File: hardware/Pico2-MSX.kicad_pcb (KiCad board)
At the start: 4 copper layers, 82.9 x 64.6 mm, 63 parts, among them J1 DEBUG, J2 USB_C, SW1 BOOT, U1 MCP4922-ESL, U2 TXB0108PW, U3 W25Q128JVS, U4 W25Q128JVS, U6 RP2350_80QFN, U7 MC74LCX32DTR2G, U8 AMS1117-3.3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

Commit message: Improving the 1v1 circuit
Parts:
- C16, C17: footprint Capacitor_SMD:C_0603_1608Metric -> Additional:C_0603_1608Metric_small
- L1: footprint Inductor_SMD:L_1008_2520Metric -> Additional:L_pol_2016
- moved L1 0.86 mm to (160.1, 80.7)
- moved C17 0.72 mm to (160.1, 82.8)
- moved D3 0.27 mm to (193.5, 87.8)
- moved TP3 0.14 mm to (159.1, 85.2)
- moved C16 0.13 mm to (160.1, 84.5)
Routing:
- net +3V3: track 255.8 -> 258.9 mm
- net +1V1: track 38.1 -> 36.9 mm
- net /VREG_LX: track 5.93 -> 5.18 mm
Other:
- outline, holes or cut-outs redrawn

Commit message: Some optimizations
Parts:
- added kibuzzard-671CD351: G***, kibuzzard-671CD351, F.Cu at (122.1, 81.5)
- added kibuzzard-671CD378: G***, kibuzzard-671CD378, F.Cu at (122.1, 92.6)
- added kibuzzard-671CD39D: G***, kibuzzard-671CD39D, B.Cu at (159.1, 87.6)
- added kibuzzard-671CD496: G***, kibuzzard-671CD496, B.Cu at (125.7, 71.7)
- moved C19 0.20 mm to (163.5, 87.3)
- moved C20 0.20 mm to (163.5, 90.5)
- moved C21 0.20 mm to (163.5, 91.3)
- moved C22 0.20 mm to (163.5, 94.8)
- moved C5 0.20 mm to (150.7, 88.7)
- moved C6 0.20 mm to (150.7, 90.7)
- moved C7 0.20 mm to (150.7, 92.7)
- moved C10 0.20 mm to (154.5, 97.3)
- moved C11 0.20 mm to (154.9, 84.5)
- moved C12 0.20 mm to (156.5, 97.3)
- moved C13 0.20 mm to (157.7, 84.5)
- moved C14 0.20 mm to (157.8, 97.3)
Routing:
- net +3V3: track 258.9 -> 257.1 mm
- net +1V1: track 36.9 -> 36.3 mm

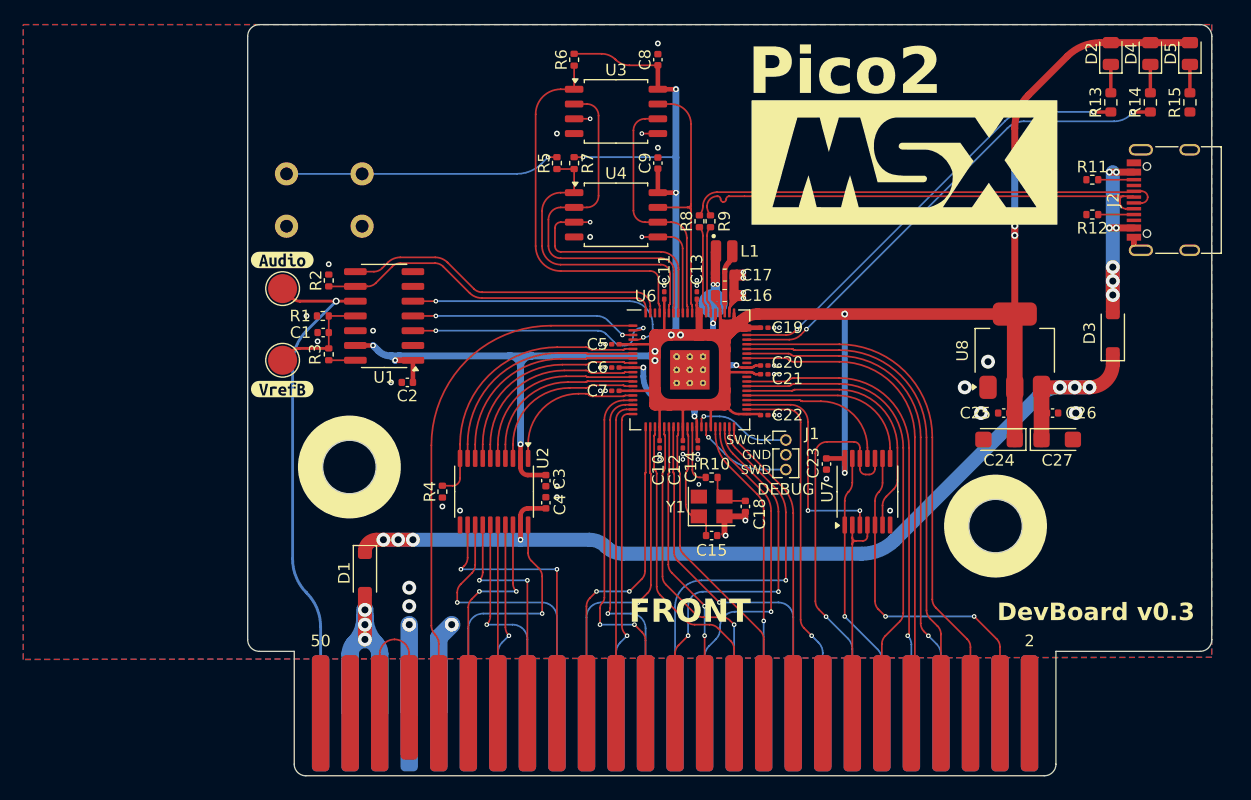
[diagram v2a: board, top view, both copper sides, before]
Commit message: Delete via for flash memory
And other small modifications (reference at JLCPCB)
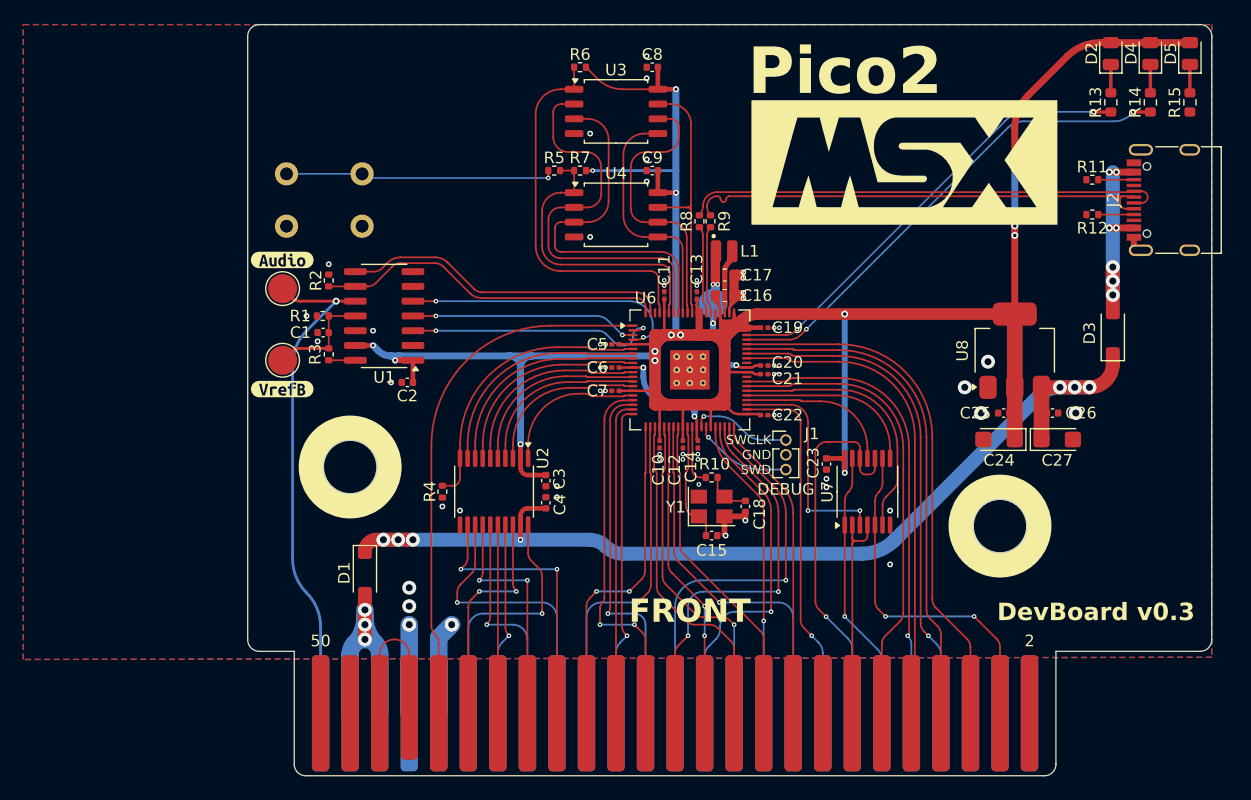
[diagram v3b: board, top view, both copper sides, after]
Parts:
- moved R6 0.82 mm to (147.7, 64.9), turned to 180 degrees
- moved R7 0.82 mm to (147.7, 73.8), turned to 180 degrees
- moved C8 0.80 mm to (153.9, 64.9), turned to 180 degrees
- moved C9 0.80 mm to (153.9, 73.8), turned to 180 degrees
- moved R5 0.68 mm to (145.5, 73.8), turned to 180 degrees
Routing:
- net /QSPI_SD1: track 32.7 -> 35.6 mm
- net /QSPI_SCLK: track 21.8 -> 24.7 mm
- net /QSPI_SD0: track 19.8 -> 21.3 mm, vias 2 -> 0
- net /QSPI_SD2: track 30.5 -> 32.0 mm, vias 2 -> 0
- net +3V3: track 257.1 -> 256.0 mm
- net GND: vias 54 -> 58
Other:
- outline, holes or cut-outs redrawn

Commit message: Cost reduction and correction of fixing hole placement
- The via are now at a minimum hole size of 0.25.
- The 0201 capacitors have been replaced by 0402s.
- The fixing holes have been moved to a position closer to the standard.
- The tracks have been widened outside the RP2350 area.
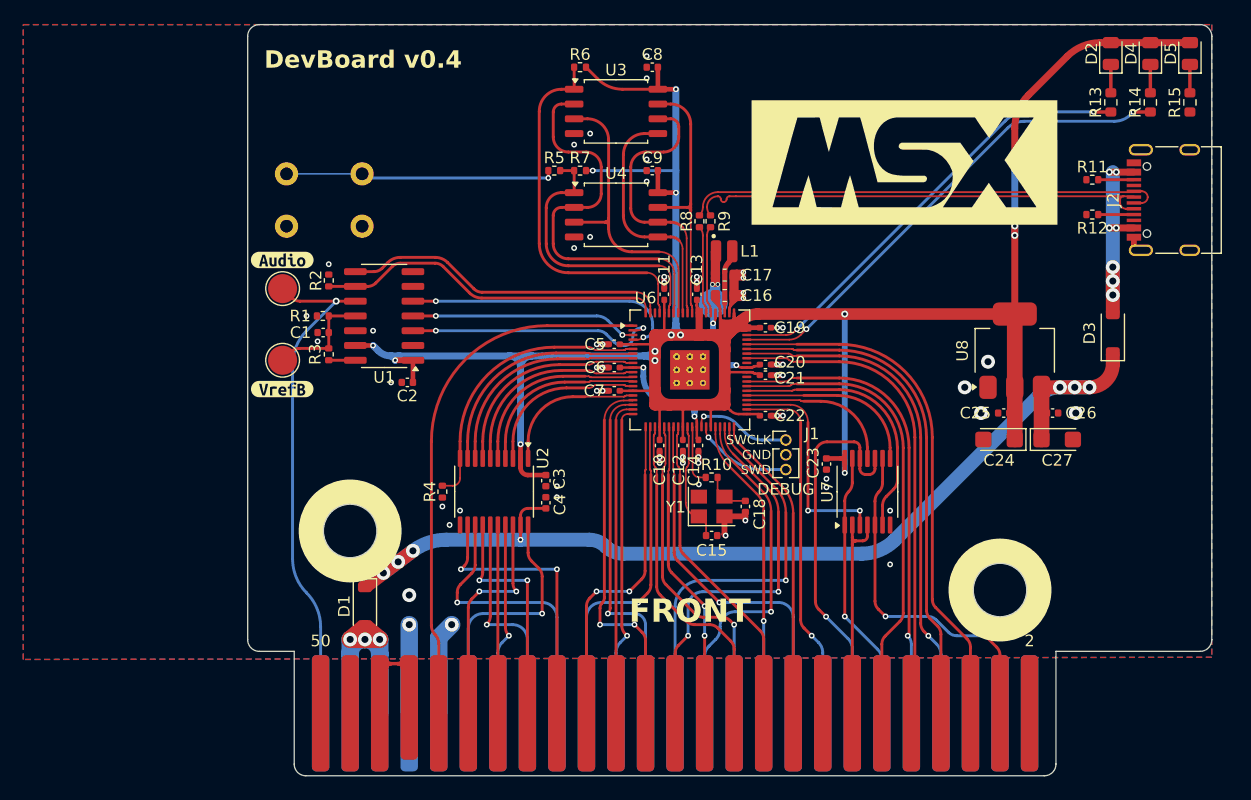
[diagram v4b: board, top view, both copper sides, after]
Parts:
- C10, C11, C12, C13, C14, C19, C20, C21, C22, C5, C6, C7: footprint Capacitor_SMD:C_0201_0603Metric -> Additional:C_0402_1005Metric_thin
- moved D1 2.86 mm to (129.2, 111.2)
- moved C21 0.13 mm to (163.6, 91.4)
- moved C20 0.13 mm to (163.6, 90.5)
- moved C22 0.11 mm to (163.6, 94.9)
- moved C14 0.11 mm to (157.9, 97.4)
- moved C19 0.10 mm to (163.6, 87.3)
- moved C11 0.10 mm to (154.9, 84.4)
- moved C13 0.10 mm to (157.7, 84.4)
- moved C10 0.10 mm to (154.5, 97.4)
- moved C12 0.10 mm to (156.5, 97.4)
- moved C5 0.10 mm to (150.6, 88.7)
- moved C6 0.10 mm to (150.6, 90.7)
- moved C7 0.10 mm to (150.6, 92.7)
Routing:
- net Net-(U5-SW1): track 13.5 -> 0.00 mm
- net GND: track 29.9 -> 41.1 mm, vias 58 -> 60
- net /QSPI_SD2: track 32.0 -> 27.0 mm
- net +5V: track 88.4 -> 89.7 mm
- net /QSPI_SD1: track 35.6 -> 34.8 mm
- net /QSPI_SS1: track 32.7 -> 31.9 mm
- net /QSPI_SS0: track 25.5 -> 24.7 mm
- net Net-(D1-A): track 25.9 -> 25.2 mm
- net /~{SLTSL}: track 30.9 -> 30.4 mm
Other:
- outline, holes or cut-outs redrawn
- board text added: "DevBoard v0.4"
- board text removed: "DevBoard v0.3"
